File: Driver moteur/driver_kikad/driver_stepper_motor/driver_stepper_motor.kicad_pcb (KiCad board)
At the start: 2 copper layers, 77 x 54 mm, 48 parts, among them Con1 OutMot, Con2 Conn_01x04, U1 STM32G031G8U6

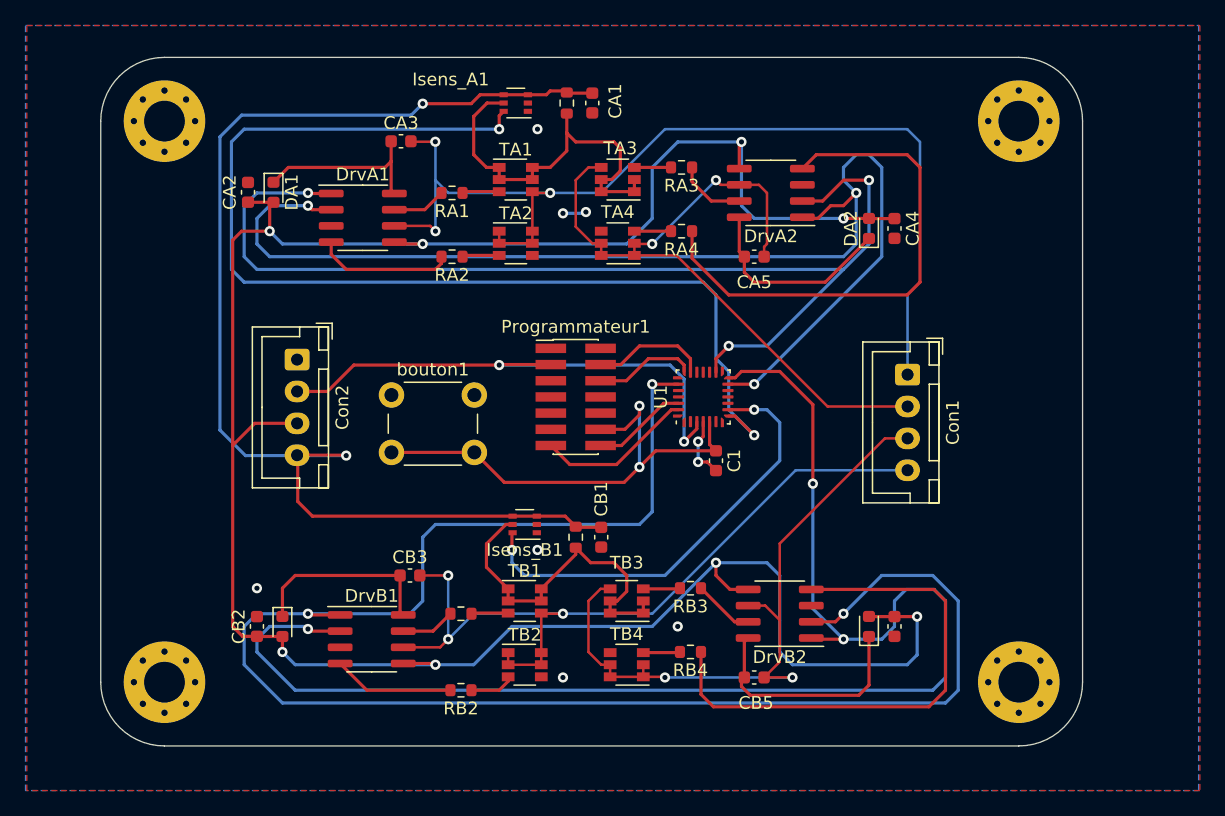
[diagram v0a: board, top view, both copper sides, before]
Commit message: PCB root sans erreurs
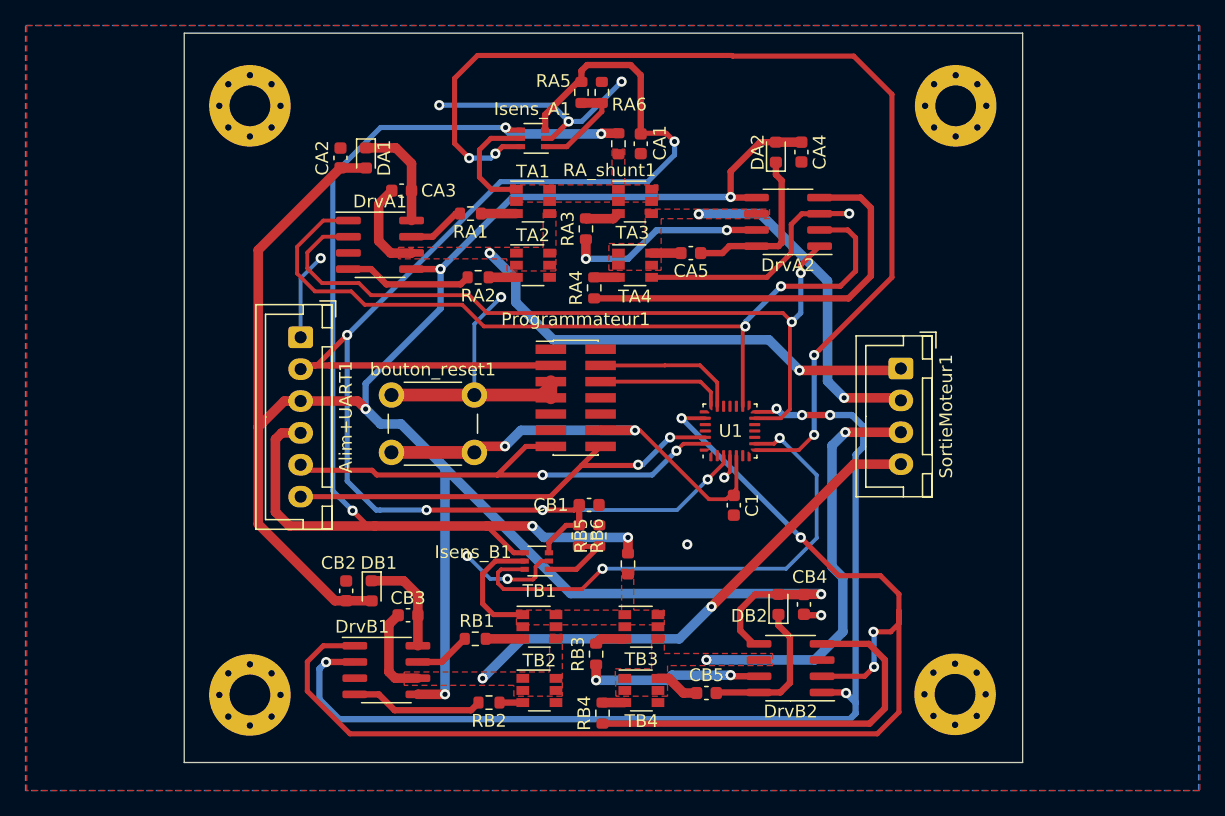
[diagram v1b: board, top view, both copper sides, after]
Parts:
- removed Con2: Conn_01x04, Connector_JST:JST_XH_B4B-XH-A_1x04_P2.50mm_Vertical
- added Alim+UART1: Conn_01x06, Connector_JST:JST_XH_B6B-XH-A_1x06_P2.50mm_Vertical, F.Cu at (65.7, 153.9)
- added RA5: 100k, Resistor_SMD:R_0603_1608Metric, F.Cu at (89.3, 134.8)
- added RA6: 100k, Resistor_SMD:R_0603_1608Metric, F.Cu at (87.7, 134.8)
- added RB5: 100k, Resistor_SMD:R_0603_1608Metric, F.Cu at (89.1, 169.5)
- added RB6: 100k, Resistor_SMD:R_0603_1608Metric, F.Cu at (87.5, 169.5)
- RA_shunt1, RB_shunt1: value à déterminer -> 0,75m
- moved CA4 9.44 mm to (105.0, 139.4)
- moved DA2 9.44 mm to (103.0, 139.4)
- moved RB3 9.03 mm to (88.8, 178.8), turned to 90 degrees
- moved RA3 8.92 mm to (88.0, 145.4), turned to 90 degrees
- moved RB4 8.40 mm to (89.3, 183.4), turned to 90 degrees
- moved RA4 8.17 mm to (88.7, 150.1), turned to 90 degrees
- moved CA2 7.73 mm to (68.8, 139.9)
- moved DA1 7.73 mm to (70.8, 139.9)
- moved CB2 7.54 mm to (69.2, 173.8)
- moved DB1 7.54 mm to (71.2, 173.8)
- moved CB4 7.31 mm to (105.2, 174.9)
- moved DB2 7.31 mm to (103.2, 174.9)
- moved H2 6.81 mm to (61.7, 135.8)
- moved H4 6.77 mm to (61.7, 182.0)
- moved RA_shunt1 5.16 mm to (90.6, 138.8)
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- renumbered Con1 to SortieMoteur1, bouton1 to bouton_reset1
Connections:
- CA1 pad 2: 24V -> 3,3V
- CB1 pad 2: 24V -> 3,3V
- Isens_A1 pad 1: GND -> Net-(Isens_A1-Pad1)
- Isens_A1 pad 3: 24V -> 3,3V
- Isens_B1 pad 1: GND -> Net-(Isens_B1-Pad1)
- Isens_B1 pad 3: 24V -> 3,3V
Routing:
- net 3,3V: track 42.6 -> 127.0 mm, vias 2 -> 5
- net GND: track 7.17 -> 78.4 mm, vias 9 -> 11
- net /Phase_A/A+: track 80.9 -> 44.5 mm, vias 3 -> 2
- net PWMB: track 134.8 -> 99.3 mm, vias 3 -> 4
- net PWMA_IN: track 94.7 -> 61.5 mm, vias 3 -> 2
- net /Phase_A/A-: track 57.4 -> 28.8 mm
- net Tx: track 7.48 -> 35.8 mm, vias 0 -> 2
- net PWMB_IN: track 110.8 -> 83.1 mm, vias 3 -> 5
- net Rx: track 12.4 -> 38.2 mm, vias 0 -> 2
- net Net-(Isens_A1-Pad5): track 31.6 -> 9.07 mm
- net PWMA: track 86.4 -> 66.5 mm, vias 3 -> 2
- net Net-(Isens_B1-Pad5): track 28.0 -> 9.57 mm
- net /Phase_B/B-: track 54.0 -> 36.3 mm
- net /Phase_B/B+: track 61.8 -> 47.0 mm, vias 3 -> 2
- net 12V: track 188.0 -> 177.5 mm, vias 8 -> 5
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- added copper zone on F.Cu, net /Phase_A/A+
- added copper zone on F.Cu, net /Phase_A/A-
- added copper zone on F.Cu, net /Phase_B/B+
- added copper zone on F.Cu, net /Phase_B/B-
- added copper zone on F.Cu, net Net-(Isens_A1-Pad5)
- added copper zone on F.Cu, net Net-(Isens_B1-Pad5)
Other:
- board size 77 x 54 mm -> 65.8 x 57.2 mm

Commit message: modif push button
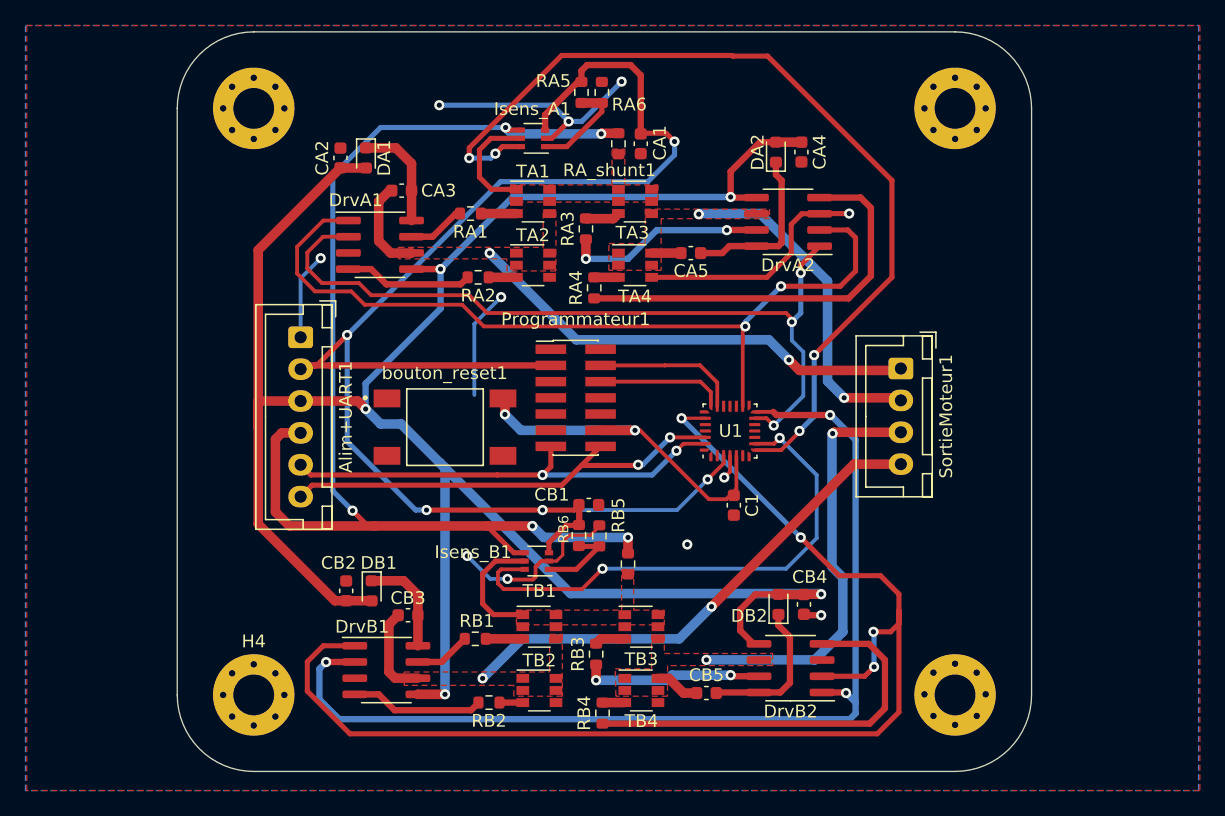
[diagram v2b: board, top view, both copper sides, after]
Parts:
- bouton_reset1: footprint Button_Switch_THT:SW_PUSH_6mm -> 2-1437565-7:SW_2-1437565-7
- moved bouton_reset1 4.90 mm to (77.0, 161.0)
- moved H2 0.36 mm to (62.0, 136.0)
- moved H4 0.30 mm to (62.0, 182.0)
- moved H1 0.21 mm to (117.0, 136.0)
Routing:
- net ADC_A: track 81.8 -> 72.2 mm
- net GND: track 78.4 -> 70.1 mm
- net NRST: track 35.7 -> 27.9 mm
- net Rx: track 38.2 -> 35.6 mm
- net 3,3V: track 127.0 -> 125.1 mm
- net PWMB_IN: track 83.1 -> 81.4 mm, vias 5 -> 3
- net PWMA_IN: track 61.5 -> 62.9 mm, vias 2 -> 3
- net 12V: track 177.5 -> 178.7 mm
- net /Phase_A/A+: track 44.5 -> 43.6 mm
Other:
- board size 65.8 x 57.2 mm -> 67 x 58 mm
